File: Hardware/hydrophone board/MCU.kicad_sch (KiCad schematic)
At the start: 2 parts, among them J401 Conn_01x07, U401 DEV-16771

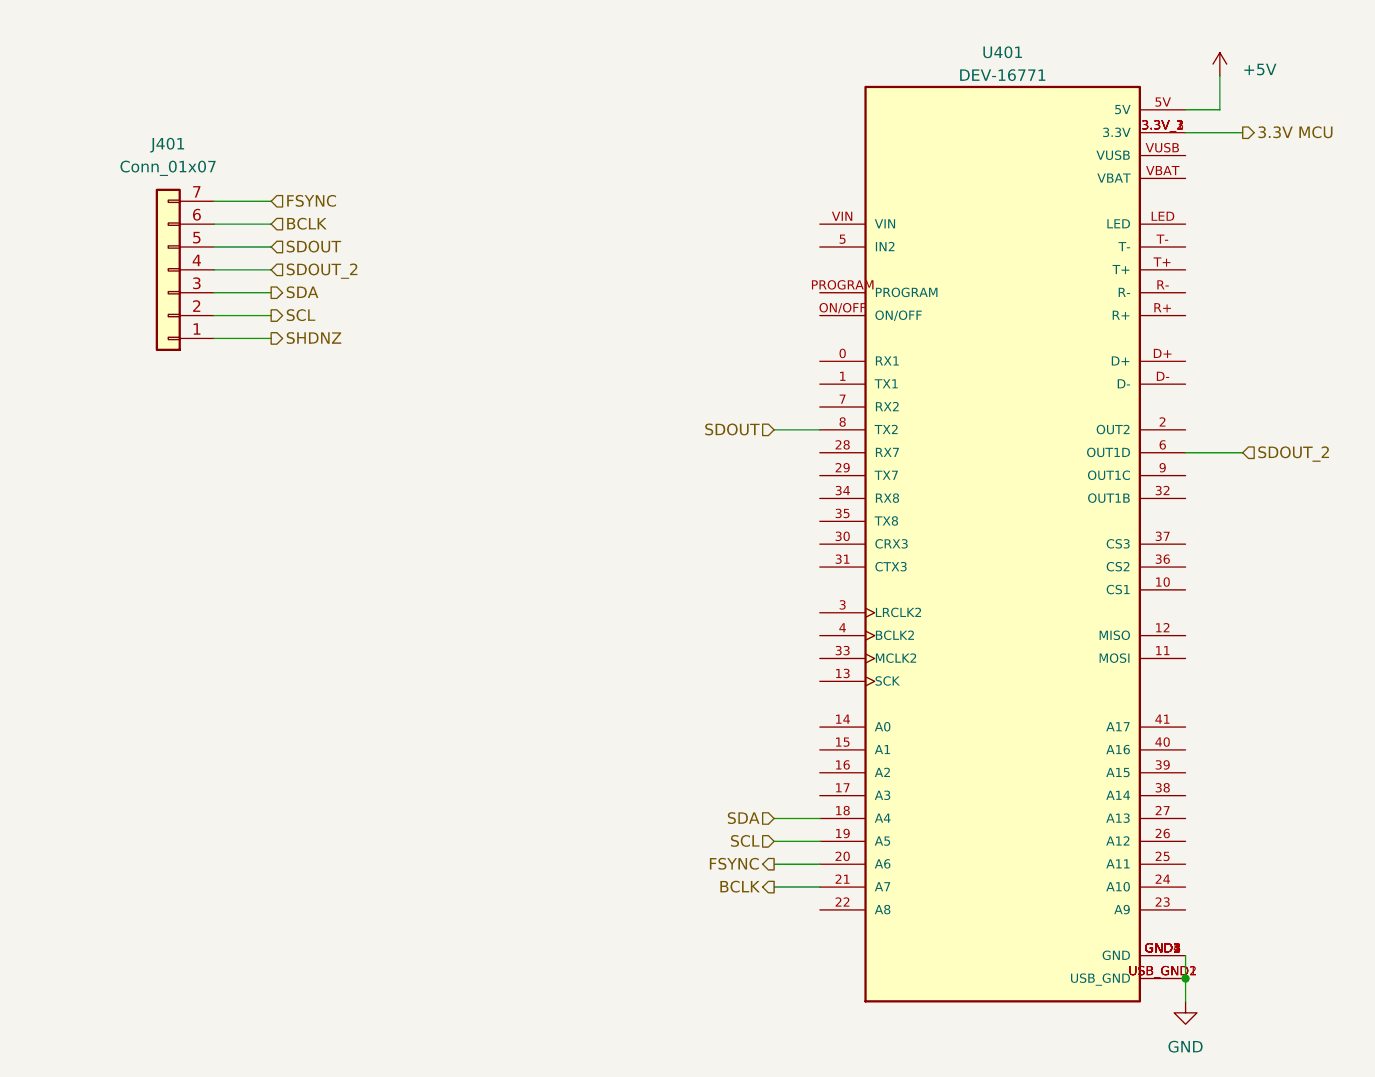
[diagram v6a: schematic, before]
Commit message: resolved ERC errors and changed mic bias resistor for 3.3V
1.1k -> 360 ohm
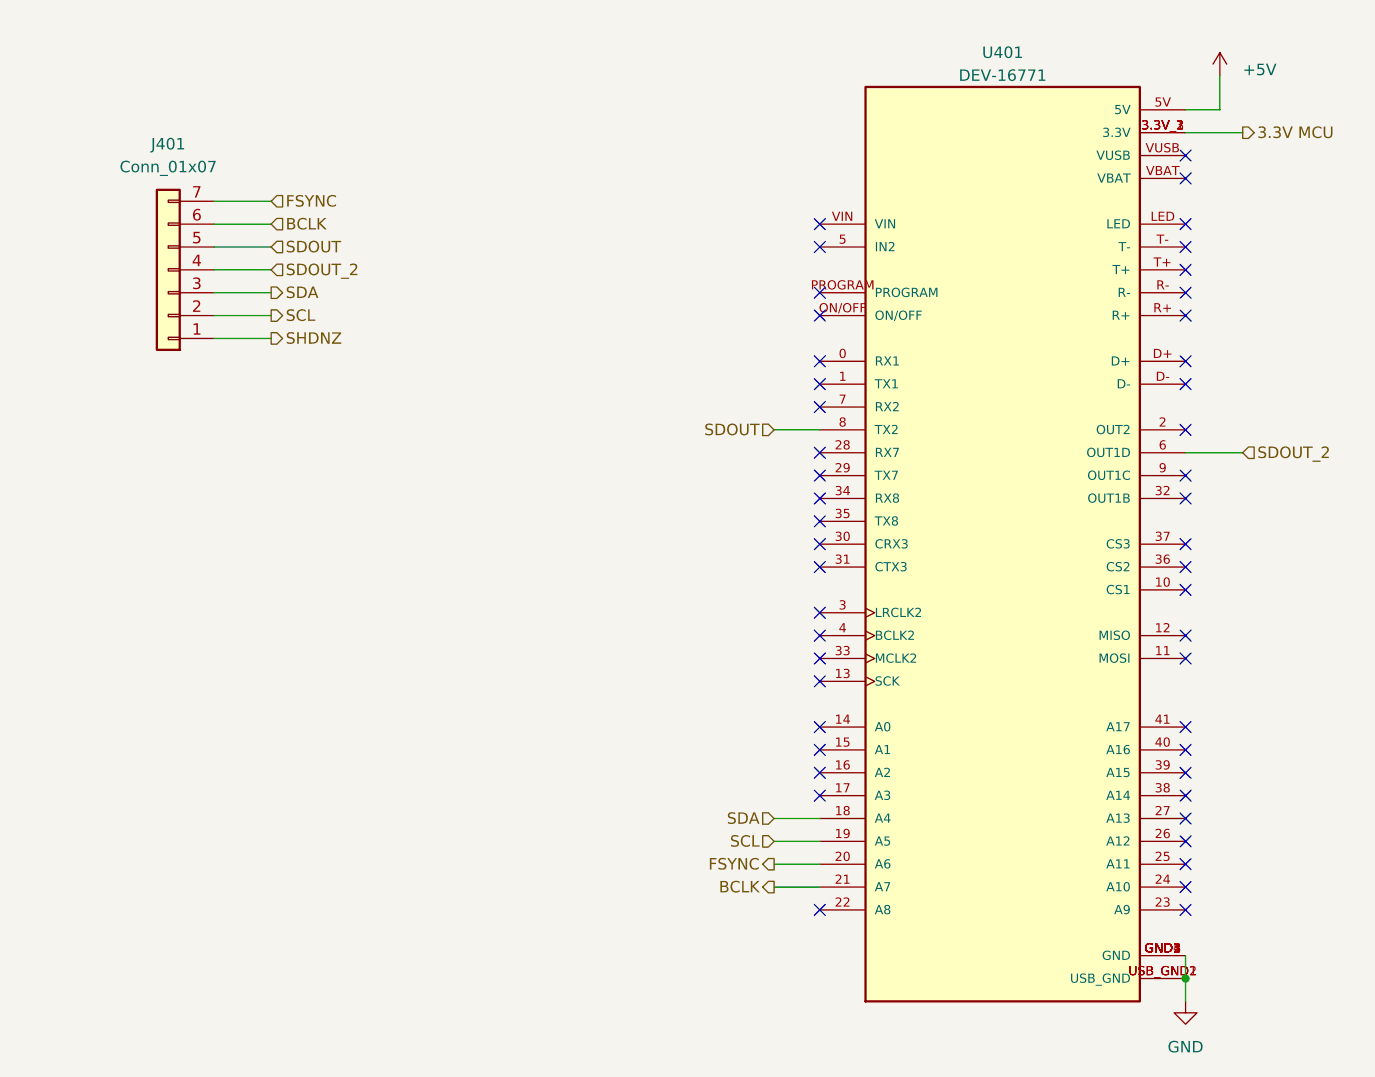
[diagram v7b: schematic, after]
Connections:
- no-connect marks 0 -> 48
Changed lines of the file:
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@@
   (junction (at 187.96 137.16) (diameter 0) (color 0 0 0 0)
   )
+  (no_connect (at 187.96 121.92))
+  (no_connect (at 187.96 63.5))
+  (no_connect (at 147.32 99.06))
+  (no_connect (at 187.96 88.9))
+  (no_connect (at 147.32 104.14))
+  (no_connect (at 187.96 55.88))
+  (no_connect (at 147.32 83.82))
+  (no_connect (at 147.32 109.22))
+  (no_connect (at 147.32 73.66))
+  (no_connect (at 147.32 114.3))
+  (no_connect (at 187.96 60.96))
+  (no_connect (at 187.96 119.38))
+  (no_connect (at 187.96 48.26))
+  (no_connect (at 147.32 91.44))
+  (no_connect (at 187.96 124.46))
+  (no_connect (at 187.96 81.28))
+  (no_connect (at 147.32 96.52))
+  (no_connect (at 187.96 116.84))
+  (no_connect (at 147.32 81.28))
+  (no_connect (at 147.32 53.34))
+  (no_connect (at 187.96 53.34))
+  (no_connect (at 147.32 88.9))
+  (no_connect (at 187.96 76.2))
+  (no_connect (at 147.32 111.76))
+  (no_connect (at 147.32 55.88))
+  (no_connect (at 187.96 99.06))
+  (no_connect (at 147.32 71.12))
+  (no_connect (at 187.96 91.44))
+  (no_connect (at 147.32 86.36))
+  (no_connect (at 147.32 63.5))
+  (no_connect (at 187.96 111.76))
+  (no_connect (at 147.32 60.96))
+  (no_connect (at 147.32 101.6))
+  (no_connect (at 187.96 45.72))
+  (no_connect (at 187.96 93.98))
+  (no_connect (at 187.96 109.22))
+  (no_connect (at 147.32 116.84))
+  (no_connect (at 187.96 114.3))
+  (no_connect (at 147.32 68.58))
+  (no_connect (at 187.96 127))
+  (no_connect (at 187.96 83.82))
+  (no_connect (at 187.96 71.12))
+  (no_connect (at 187.96 58.42))
+  (no_connect (at 147.32 78.74))
+  (no_connect (at 147.32 129.54))
+  (no_connect (at 187.96 68.58))
+  (no_connect (at 187.96 129.54))
+  (no_connect (at 187.96 101.6))
   (wire (pts (xy 80.01 63.5) (xy 86.36 63.5))
     (stroke (width 0) (type default))
